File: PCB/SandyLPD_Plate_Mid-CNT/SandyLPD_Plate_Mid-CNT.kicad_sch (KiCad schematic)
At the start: 9 parts

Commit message: WIP Top基板裏側のソケットを逃す穴を作成中。
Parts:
- SW_MACRO_L2: footprint locallib:MX-Switch-Hole-with-narrow-frame -> locallib:MX-Switch-Hole-with-narrow-frame-for-socket-escape
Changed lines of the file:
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@@
 			)
 		)
-		(property "Footprint" "locallib:MX-Switch-Hole-with-narrow-frame"
+		(property "Footprint" "locallib:MX-Switch-Hole-with-narrow-frame-for-socket-escape"
 			(at 83.82 28.575 0)
 			(effects

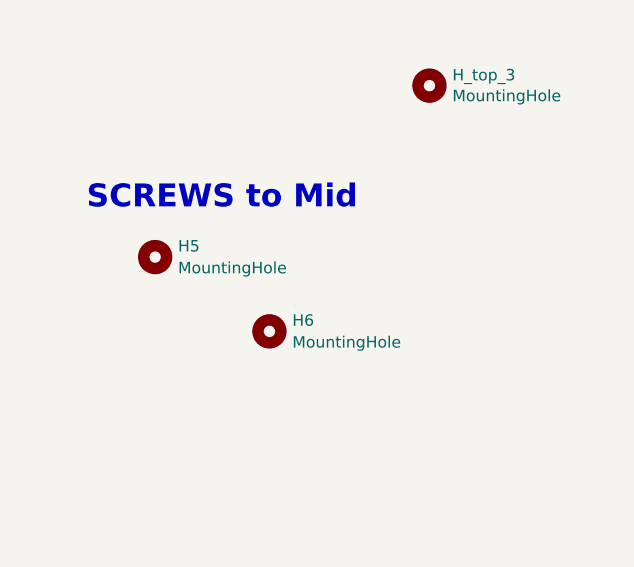
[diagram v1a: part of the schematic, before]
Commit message: Mid-CNTのプレート固定用スルーホールタップを1個減らす
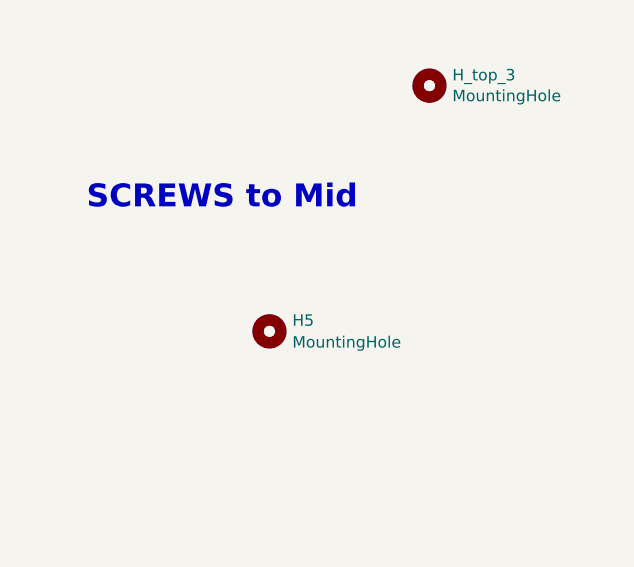
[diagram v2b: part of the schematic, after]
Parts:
- removed H5: MountingHole, MountingHole:MountingHole_2.2mm_M2, symbol Mechanical:MountingHole
- renumbered H6 to H5
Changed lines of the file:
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@@
 		(dnp no)
 		(fields_autoplaced yes)
-		(property "Reference" "H6"
+		(property "Reference" "H5"
 			(at 43.815 121.3428 0)
 			(effects
@@
 			(project "SandyLPD_Mid-CNT"
 				(path "/a99ab643-cdc7-4f8c-8088-c1f4faa914d1"
-					(reference "H6")
-					(unit 1)
-				)
-			)
-		)
-	)
-	(symbol
-		(lib_id "Mechanical:MountingHole")
-		(at 28.575 114.3 0)
-		(unit 1)
-		(exclude_from_sim yes)
-		(in_bom no)
-		(on_board yes)
-		(dnp no)
-		(fields_autoplaced yes)
-		(property "Reference" "H5"
-			(at 31.115 113.0878 0)
-			(effects
-				(font
-					(size 1.27 1.27)
-				)
-				(justify left)
-			)
-		)
-		(property "Value" "MountingHole"
-			(at 31.115 115.5121 0)
-			(effects
-				(font
-					(size 1.27 1.27)
-				)
-				(justify left)
-			)
-		)
-		(property "Footprint" "MountingHole:MountingHole_2.2mm_M2"
-			(at 28.575 114.3 0)
-			(effects
-				(font
-					(size 1.27 1.27)
-				)
-				(hide yes)
-			)
-		)
-		(property "Datasheet" "~"
-			(at 28.575 114.3 0)
-			(effects
-				(font
-					(size 1.27 1.27)
-				)
-				(hide yes)
-			)
-		)
-		(property "Description" "Mounting Hole without connection"
-			(at 28.575 114.3 0)
-			(effects
-				(font
-					(size 1.27 1.27)
-				)
-				(hide yes)
-			)
-		)
-		(instances
-			(project ""
-				(path "/a99ab643-cdc7-4f8c-8088-c1f4faa914d1"
 					(reference "H5")
